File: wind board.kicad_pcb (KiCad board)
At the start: 2 copper layers, 70.1 x 65.1 mm, 131 parts, among them J1 USB_C_Receptacle_USB2.0_14P, J2 Conn_01x06_MountingPin, J3 Conn_01x06_MountingPin, J4 12V -, J5 12V +, J6 Conn_01x06_MountingPin, Q1 AONR21321, U1 CH334R, U10 AT24C512C-SSHM, U11 XC6206PxxxMR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

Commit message: new buck
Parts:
- moved G*** 12.1 mm to (160.2, 89.5)
- moved C50 3.75 mm to (138.0, 53.8)
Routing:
- net ~: track 117.9 -> 122.1 mm
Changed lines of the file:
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@@
 		(sheetname "/")
 		(sheetfile "wind board.kicad_sch")
-		(attr exclude_from_pos_files)
+		(attr exclude_from_pos_files exclude_from_bom)
 		(fp_line
 			(start -0.7 -0.7)
@@
 		(sheetname "/")
 		(sheetfile "wind board.kicad_sch")
-		(attr smd exclude_from_pos_files)
+		(attr smd exclude_from_pos_files exclude_from_bom)
 		(fp_line
 			(start -2.875 -5.325)
@@
 		(sheetname "/Power Input/")
 		(sheetfile "power_input.kicad_sch")
-		(attr exclude_from_pos_files)
+		(attr exclude_from_pos_files exclude_from_bom)
 		(fp_circle
 			(center 0 0)
@@
 		(sheetname "/")
 		(sheetfile "wind board.kicad_sch")
-		(attr exclude_from_pos_files)
+		(attr exclude_from_pos_files exclude_from_bom)
 		(fp_line
 			(start -0.7 -0.7)
@@
 		(sheetname "/")
 		(sheetfile "wind board.kicad_sch")
-		(attr exclude_from_pos_files)
+		(attr exclude_from_pos_files exclude_from_bom)
 		(fp_line
 			(start -0.7 -0.7)
@@
 	(footprint "Capacitor_SMD:C_0402_1005Metric"
 		(layer "F.Cu")
-		(at 134.25 53.8 -90)
+		(at 138 53.8 -90)
 		(descr "Capacitor SMD 0402 (1005 Metric), square (rectangular) end terminal, IPC-7351 nominal, (Body size source: IPC-SM-782 page 76, https://www.pcb-3d.com/wordpress/wp-content/uploads/ipc-sm-782a_amendment_1_and_2.pdf), generated with kicad-footprint-generator")
 		(tags "capacitor")
 		(property "Reference" "C50"
-			(at 0 -1.16 90)
+			(at 0 1 90)
 			(layer "F.SilkS")
 			(effects
@@
 		(sheetname "/")
 		(sheetfile "wind board.kicad_sch")
-		(attr exclude_from_pos_files)
+		(attr exclude_from_pos_files exclude_from_bom)
 		(fp_line
 			(start -0.7 -0.7)
@@
 			(at -0.1 -3.9 90)
 			(layer "F.SilkS")
+			(hide yes)
 			(effects
 				(font
@@
 		(tags "capacitor")
 		(property "Reference" "C22"
-			(at -0.125 -3.4 90)
+			(at 2.8 0.05 90)
 			(layer "F.SilkS")
+			(hide yes)
 			(effects
 				(font
@@
 		(sheetname "/")
 		(sheetfile "wind board.kicad_sch")
-		(attr smd exclude_from_pos_files)
+		(attr smd exclude_from_pos_files exclude_from_bom)
 		(fp_line
 			(start -2.875 -5.325)
@@
 		(tags "test point THT pad rectangle square")
 		(property "Reference" "TP10"
-			(at 2.9 0.5 0)
+			(at -1.7 -1.85 0)
 			(layer "F.SilkS")
 			(effects
@@
 		(sheetname "/")
 		(sheetfile "wind board.kicad_sch")
-		(attr exclude_from_pos_files)
+		(attr exclude_from_pos_files exclude_from_bom)
 		(fp_line
 			(start -0.7 -0.7)
@@
 		(tags "TSSOP SO")
 		(property "Reference" "U4"
-			(at 0 -4.2 90)
+			(at 0 4.15 90)
 			(layer "F.SilkS")
 			(effects
@@
 		(tags "TSSOP SO")
 		(property "Reference" "U8"
-			(at 0 -4.2 90)
+			(at 1.35 4.125 90)
 			(layer "F.SilkS")
 			(effects
@@
 		(tags "capacitor")
 		(property "Reference" "C1"
-			(at 1.78 0 90)
+			(at 1.7 0 90)
 			(layer "F.SilkS")
 			(effects
@@
 		(sheetname "/")
 		(sheetfile "wind board.kicad_sch")
-		(attr exclude_from_pos_files)
+		(attr exclude_from_pos_files exclude_from_bom)
 		(fp_line
 			(start -0.7 -0.7)
@@
 			)
 		)
+		(property "LCSC" "C91552"
+			(at 0 0 0)
+			(layer "F.SilkS")
+			(hide yes)
+			(effects
+				(font
+					(size 1.27 1.27)
+					(thickness 0.15)
+				)
+			)
+		)
 		(property ki_fp_filters "Connector*:*_1x??_*")
 		(sheetname "/")
 		(sheetfile "wind board.kicad_sch")
-		(attr through_hole)
+		(attr through_hole exclude_from_pos_files exclude_from_bom)
 		(fp_line
 			(start 4.15 -1.38)
@@
 		(tags "test point THT pad rectangle square")
 		(property "Reference" "TP8"
-			(at 0 -1.448 0)
+			(at -2.35 0 0)
 			(layer "F.SilkS")
 			(effects
@@
 		(sheetname "/")
 		(sheetfile "wind board.kicad_sch")
-		(attr exclude_from_pos_files)
+		(attr exclude_from_pos_files exclude_from_bom)
 		(fp_line
 			(start -0.7 -0.7)
@@
 		(sheetname "/")
 		(sheetfile "wind board.kicad_sch")
-		(attr exclude_from_pos_files)
+		(attr exclude_from_pos_files exclude_from_bom)
 		(fp_line
 			(start -0.7 -0.7)
@@
 		(sheetname "/")
 		(sheetfile "wind board.kicad_sch")
-		(attr exclude_from_pos_files)
+		(attr exclude_from_pos_files exclude_from_bom)
 		(fp_line
 			(start -0.7 -0.7)
@@
 		(sheetname "/")
 		(sheetfile "wind board.kicad_sch")
-		(attr exclude_from_pos_files)
+		(attr exclude_from_pos_files exclude_from_bom)
 		(fp_line
 			(start -0.7 -0.7)
@@
 		(sheetname "/")
 		(sheetfile "wind board.kicad_sch")
-		(attr exclude_from_pos_files)
+		(attr exclude_from_pos_files exclude_from_bom)
 		(fp_line
 			(start -0.7 -0.7)
@@
 		(sheetname "/")
 		(sheetfile "wind board.kicad_sch")
-		(attr smd exclude_from_pos_files)
+		(attr smd exclude_from_pos_files exclude_from_bom)
 		(fp_line
 			(start -2.875 -5.325)
@@
 		(sheetname "/")
 		(sheetfile "wind board.kicad_sch")
-		(attr exclude_from_pos_files)
+		(attr exclude_from_pos_files exclude_from_bom)
 		(fp_line
 			(start -0.7 -0.7)
@@
 		(tags "Through hole angled pin header THT 1x03 2.54mm single row")
 		(property "Reference" "J2"
-			(at 5.05 -1.12 90)
+			(at -0.25 7.63 90)
 			(layer "F.SilkS")
 			(effects
@@
 			)
 		)
+		(property "LCSC" "C42385508"
+			(at 0 0 0)
+			(layer "F.SilkS")
+			(hide yes)
+			(effects
+				(font
+					(size 1.27 1.27)
+					(thickness 0.15)
+				)
+			)
+		)
 		(property ki_fp_filters "Connector*:*_1x??_*")
 		(sheetname "/")
 		(sheetfile "wind board.kicad_sch")
-		(attr through_hole)
+		(attr through_hole exclude_from_pos_files exclude_from_bom)
 		(fp_line
 			(start 4.15 -1.38)
@@
 		(sheetname "/Power Input/")
 		(sheetfile "power_input.kicad_sch")
-		(attr exclude_from_pos_files)
+		(attr exclude_from_pos_files exclude_from_bom)
 		(fp_circle
 			(center 0 0)
@@
 			)
 		)
+		(property "LCSC" "C42385508"
+			(at 0 0 0)
+			(layer "F.SilkS")
+			(hide yes)
+			(effects
+				(font
+					(size 1.27 1.27)
+					(thickness 0.15)
+				)
+			)
+		)
 		(property ki_fp_filters "Connector*:*_1x??_*")
 		(sheetname "/")
 		(sheetfile "wind board.kicad_sch")
-		(attr through_hole)
+		(attr through_hole exclude_from_pos_files exclude_from_bom)
 		(fp_line
 			(start 4.15 -1.38)
@@
 		(tags "test point THT pad rectangle square")
 		(property "Reference" "TP11"
-			(at -2.8 0.5 0)
+			(at 1.1 -1.8 0)
 			(layer "F.SilkS")
 			(effects
@@
 		(sheetname "/")
 		(sheetfile "wind board.kicad_sch")
-		(attr exclude_from_pos_files)
+		(attr exclude_from_pos_files exclude_from_bom)
 		(fp_line
 			(start -0.7 -0.7)
@@
 	(footprint "logos:more_cowbell"
 		(layer "B.Cu")
-		(at 159.9 101.6 180)
+		(at 160.2 89.55 180)
 		(property "Reference" "G***"
 			(at 0 0 0)
@@
 	)
 	(segment
+		(start 138 54.28)
+		(end 133.83 54.28)
+		(width 0.2)
+		(layer "F.Cu")
+		(net 2)
+	)
+	(segment
 		(start 113.602 73.9)
 		(end 115.577 71.925)
@@
 	)
 	(segment
+		(start 134.25 53.32)
+		(end 134.14 53.21)
+		(width 0.2)
+		(layer "F.Cu")
+		(net 114)
+	)
+	(segment
 		(start 155.5625 58.95)
 		(end 155.5625 60.2425)
@@
 	)
 	(segment
-		(start 139.1 55.3)
-		(end 139.55 54.85)
-		(width 0.2)
-		(layer "F.Cu")
-		(net 114)
-	)
-	(segment
 		(start 153.35 56.42)
 		(end 153.35 55.765531)
@@
 	)
 	(segment
-		(start 134.25 53.32)
-		(end 136.23 55.3)
-		(width 0.2)
-		(layer "F.Cu")
-		(net 114)
-	)
-	(segment
-		(start 136.23 55.3)
-		(end 139.1 55.3)
+		(start 134.14 53.21)
+		(end 132.05 53.21)
 		(width 0.2)
 		(layer "F.Cu")
@@
 	)
 	(segment
-		(start 132.05 53.21)
-		(end 134.14 53.21)
-		(width 0.25)
+		(start 138.02 53.32)
+		(end 139.55 54.85)
+		(width 0.2)
 		(layer "F.Cu")
 		(net 114)
@@
 	)
 	(segment
-		(start 134.14 53.21)
-		(end 134.25 53.32)
-		(width 0.25)
-		(layer "F.Cu")
-		(net 114)
-	)
-	(segment
 		(start 139.54 52.2)
 		(end 139.54 53.45)
@@
 		(width 0.2)
 		(layer "F.Cu")
+		(net 114)
+	)
+	(segment
+		(start 134.25 53.32)
+		(end 138.02 53.32)
+		(width 0.2)
+		(layer "F.Cu")

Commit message: new power supply
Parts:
- removed D5: 1N4148WS, Diode_SMD:D_SOD-323
- removed R14: 30K, Resistor_SMD:R_0603_1608Metric
- added C59: 22 uF, Capacitor_SMD:C_0402_1005Metric, F.Cu at (142.5, 101.7)
- added C60: 22 uF, Capacitor_SMD:C_0402_1005Metric, F.Cu at (144.0, 101.7)
- C25: value 10uF -> 220 nF
- C26: value 10uF -> 10 uF
- C27: value 100nF -> 1 uF
- C28: value 22uF -> 100 nF; footprint Capacitor_SMD:C_0603_1608Metric -> Capacitor_SMD:C_0402_1005Metric
- C29, C30: value 22uF -> 22 uF; footprint Capacitor_SMD:C_0603_1608Metric -> Capacitor_SMD:C_0402_1005Metric
- L1: value SPM6530T-2R2M -> SPM6530T-6R8M
- R11: value 20K -> 100k
- R12: value 30K -> 100k; footprint Resistor_SMD:R_0603_1608Metric -> Capacitor_SMD:C_0402_1005Metric
- R13: value 220K -> 24.9k; footprint Resistor_SMD:R_0603_1608Metric -> Resistor_SMD:R_0402_1005Metric
- U6: value TPS565242 -> LMR33640ADDA; footprint Package_TO_SOT_SMD:SOT6_DRL_TEX-L -> Package_SO:Texas_HSOP-8-1EP_3.9x4.9mm_P1.27mm_ThermalVias
- moved C28 15.4 mm to (131.0, 100.0), turned to 90 degrees
- moved R12 12.8 mm to (133.5, 106.0), turned to 90 degrees
- moved C25 10.6 mm to (121.5, 99.5), turned to 0 degrees
- moved C26 10.2 mm to (121.5, 98.0), turned to 0 degrees
- moved C27 7.36 mm to (125.5, 104.5), turned to 0 degrees
- moved R11 5.35 mm to (123.5, 104.5), turned to 0 degrees
- moved L1 4.30 mm to (137.0, 100.4)
- moved C30 3.81 mm to (145.5, 101.7)
- moved R13 3.45 mm to (131.0, 106.0)
- moved U6 3.30 mm to (126.3, 101.1), turned to 0 degrees
- moved G*** 1.32 mm to (122.0, 109.5)
- moved C29 0.82 mm to (147.0, 101.7)
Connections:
- C27 pad 1: /WG_+12V -> Net-(U6-VCC)
- C28 pad 1: Net-(C28-Pad1) -> Net-(U6-BOOT)
- C28 pad 2: ~ -> Net-(U6-SW)
- C29 pad 1: Net-(C28-Pad1) -> Net-(C29-Pad1)
- C30 pad 1: Net-(C28-Pad1) -> Net-(C29-Pad1)
- FB1 pad 2: Net-(C28-Pad1) -> Net-(C29-Pad1)
- L1 pad 2: Net-(C28-Pad1) -> Net-(C29-Pad1)
- R11 pad 1: /WG_+12V -> Net-(U6-PG)
- R11 pad 2: Net-(D5-K) -> Net-(U6-VCC)
- R12 pad 1: Net-(D5-K) -> Net-(C29-Pad1)
- R12 pad 2: ~ -> Net-(U6-FB)
- R13 pad 2: Net-(C28-Pad1) -> ~
- U6 pad 1: /WG_+12V -> ~
- U6 pad 2: Net-(U6-SW) -> /WG_+12V
- U6 pad 3: ~ -> /WG_+12V
- U6 pad 4: ~ -> Net-(U6-PG)
- U6 pad 5: Net-(D5-K) -> Net-(U6-FB)
- U6 pad 6: Net-(U6-FB) -> Net-(U6-VCC)
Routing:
- net Net-(C29-Pad1): track 0.00 -> 32.7 mm, vias 0 -> 2
- net Net-(C28-Pad1): track 30.2 -> 0.00 mm, vias 2 -> 0
- net /WG_+12V: track 44.2 -> 59.6 mm
- net Net-(D5-K): track 10.6 -> 0.00 mm
- net Net-(U6-VCC): track 0.00 -> 6.98 mm
- net Net-(U6-FB): track 12.7 -> 5.79 mm
- net ~: track 122.1 -> 125.5 mm, vias 108 -> 102
- net Net-(U6-BOOT): track 0.00 -> 2.01 mm
- net Net-(U6-PG): track 0.00 -> 1.79 mm
- removed copper zone on F.Cu, net Net-(U6-SW)

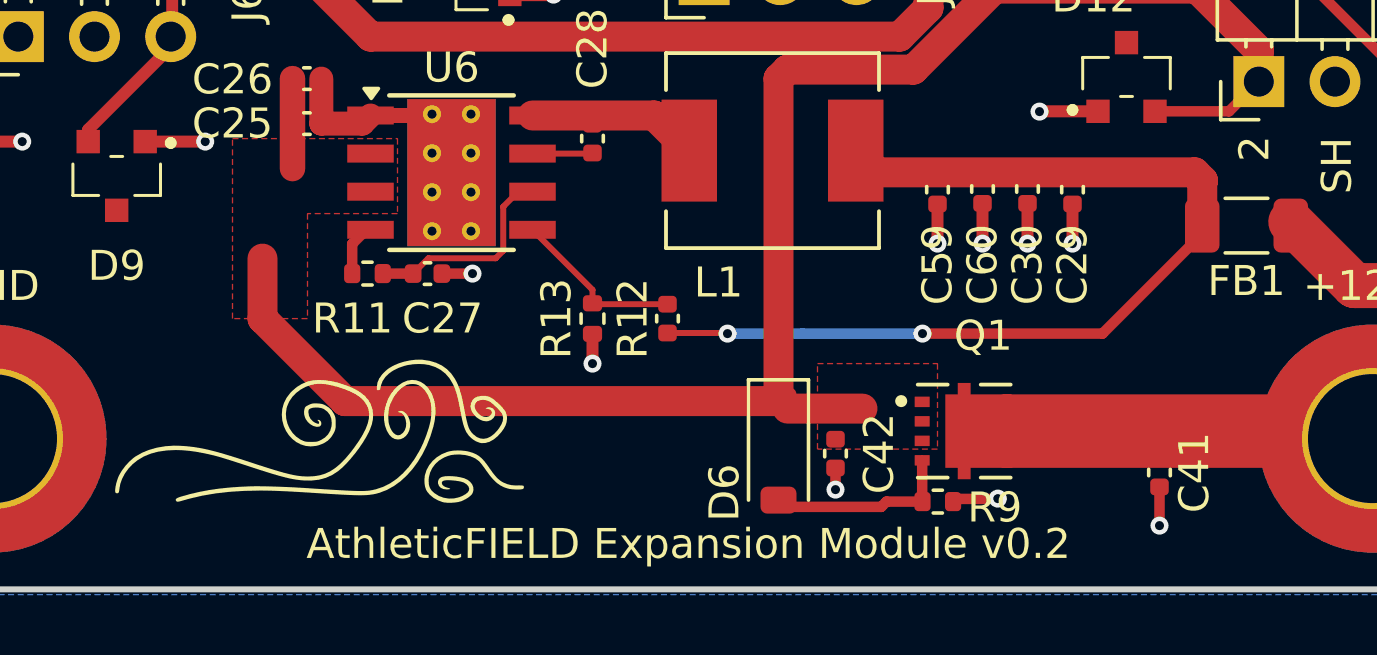
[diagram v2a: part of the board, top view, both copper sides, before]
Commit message: remove pullup resistor
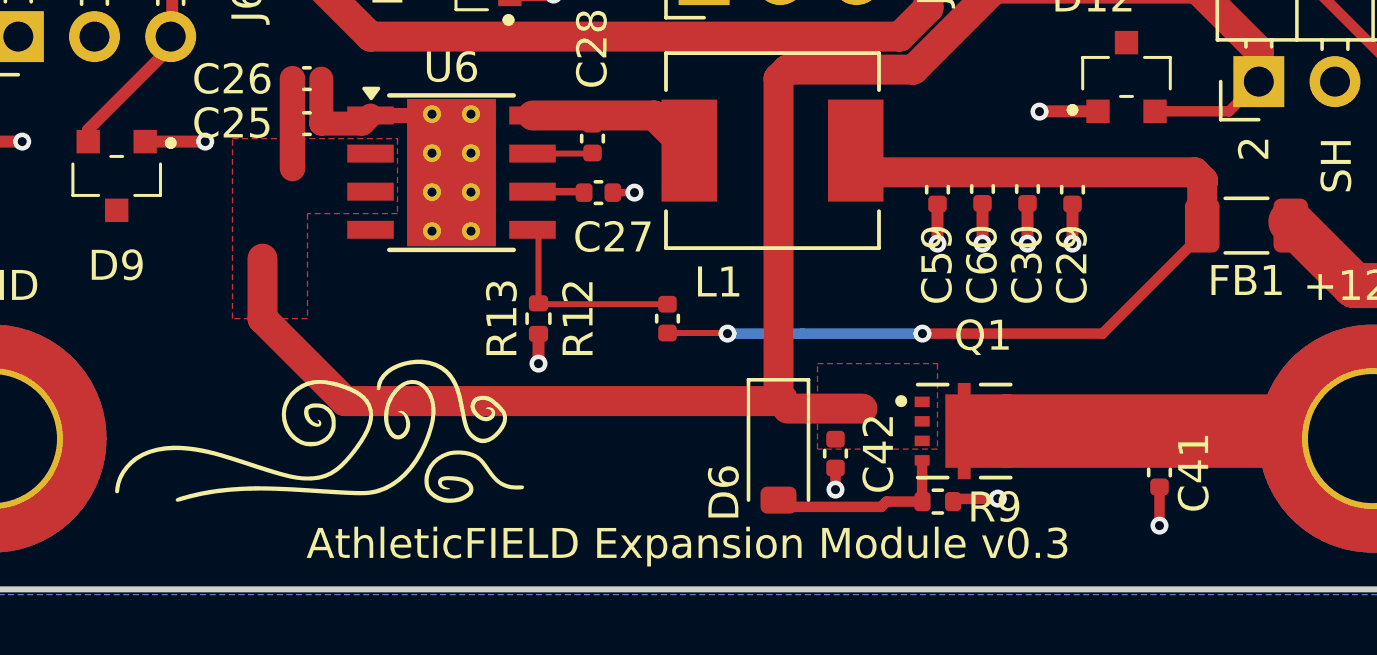
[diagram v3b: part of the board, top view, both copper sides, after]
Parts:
- removed R11: 100k, Resistor_SMD:R_0402_1005Metric
- moved C27 6.31 mm to (131.2, 101.8)
- moved R13 1.80 mm to (129.2, 106.0)
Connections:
- U6 pad 4: Net-(U6-PG) -> unconnected-(U6-PG-Pad4)
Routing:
- net Net-(U6-VCC): track 6.98 -> 1.73 mm
- net Net-(U6-PG): track 1.79 -> 0.00 mm
- net Net-(U6-FB): track 5.79 -> 6.85 mm
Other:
- board text added: "AthleticFIELD Expansion Module v0.3"
- board text removed: "AthleticFIELD Expansion Module v0.2"
